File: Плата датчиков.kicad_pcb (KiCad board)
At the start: 2 copper layers, 66 x 58.4 mm, 23 parts, among them J1 A, J2 B, J3 C

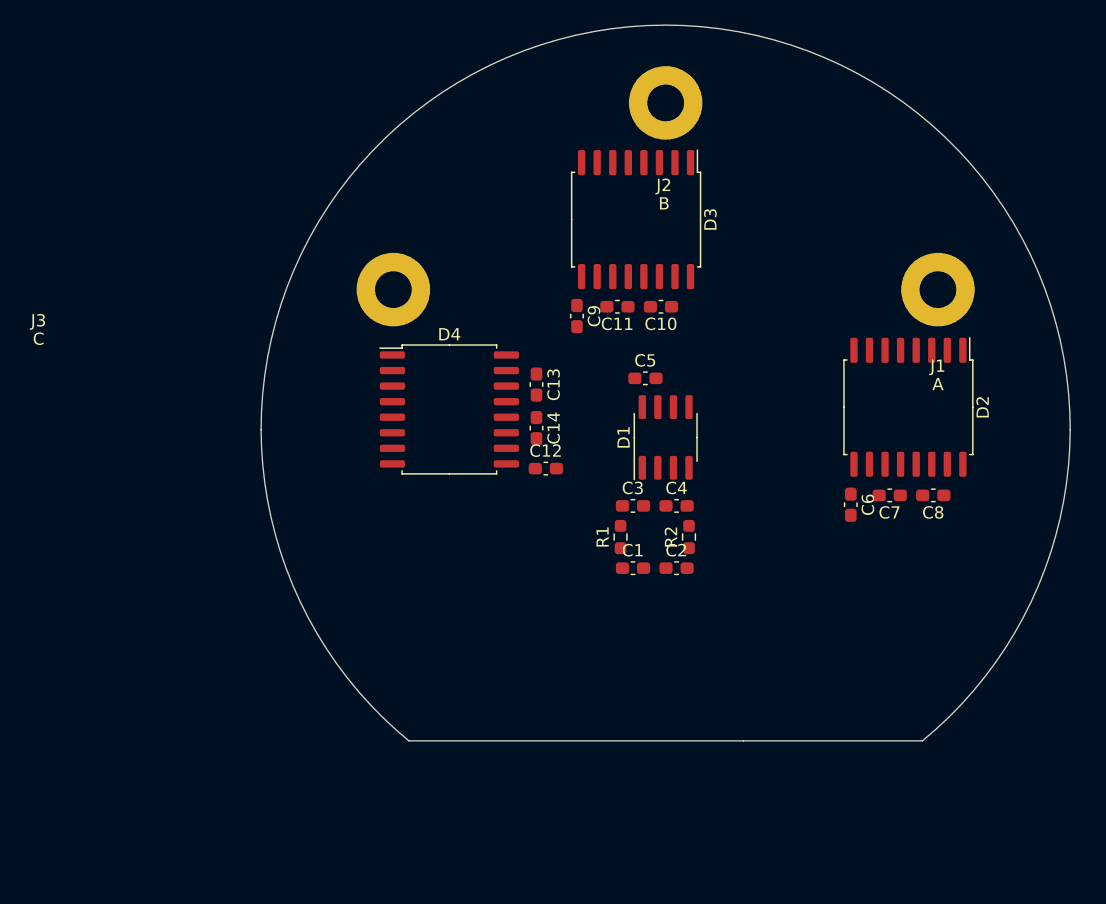
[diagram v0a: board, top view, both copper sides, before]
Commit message: Изменил контур под новую крышку
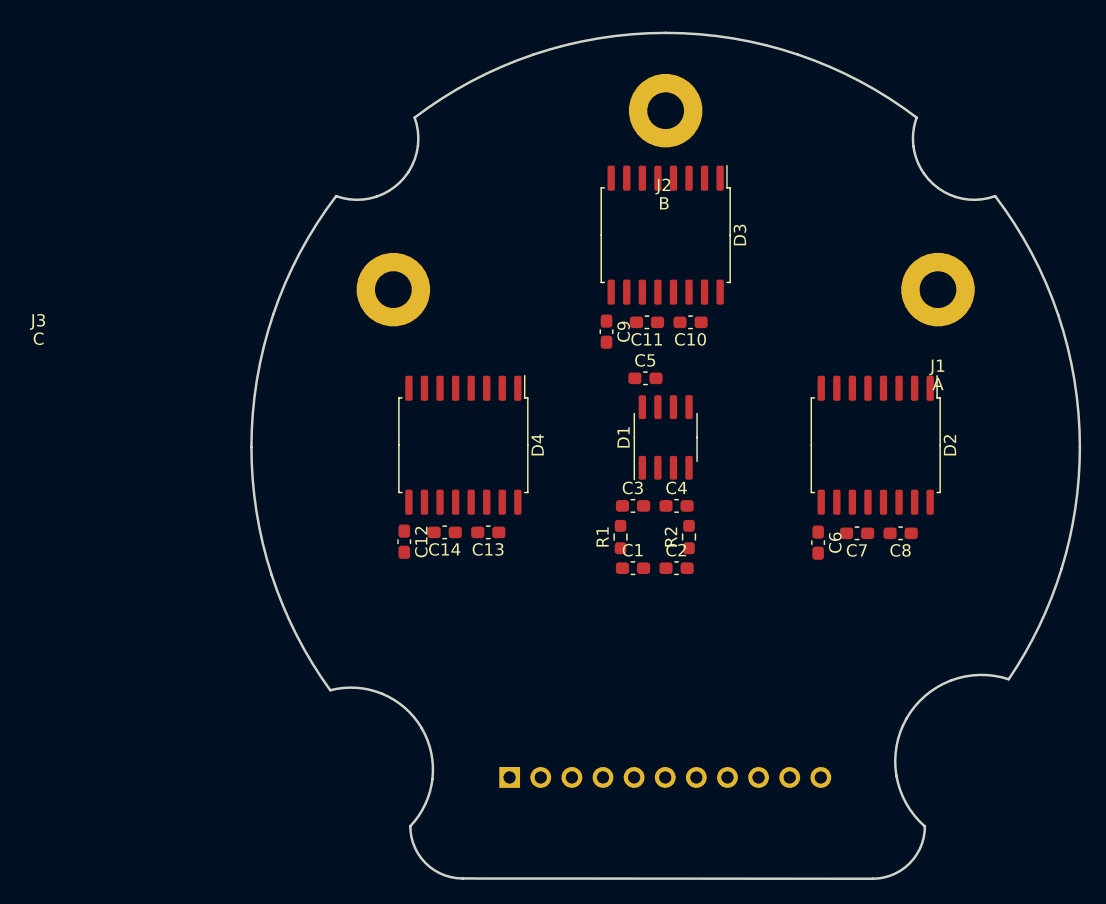
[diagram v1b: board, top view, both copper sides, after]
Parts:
- added J4: Conn_01x11, Connector_PinHeader_2.54mm:PinHeader_1x11_P2.54mm_Vertical, B.Cu at (70.5, 123.0)
- moved C12 13.0 mm to (61.8, 103.8), turned to -90 degrees
- moved C13 12.7 mm to (68.7, 103.0), turned to 180 degrees
- moved C14 11.3 mm to (65.2, 103.0), turned to 180 degrees
- moved C6 4.09 mm to (95.6, 103.8)
- moved C7 4.09 mm to (98.8, 103.1)
- moved C8 4.09 mm to (102.4, 103.1)
- moved D2 4.09 mm to (100.3, 95.9)
- moved D4 3.14 mm to (66.7, 95.9), turned to -90 degrees
- moved C10 2.73 mm to (85.2, 85.9)
- moved C11 2.73 mm to (81.7, 85.9)
- moved C9 2.73 mm to (78.4, 86.6)
- moved D3 2.73 mm to (83.2, 78.7)
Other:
- board size 66 x 58.4 mm -> 67.6 x 69 mm

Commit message: Поменял датчики на шунты
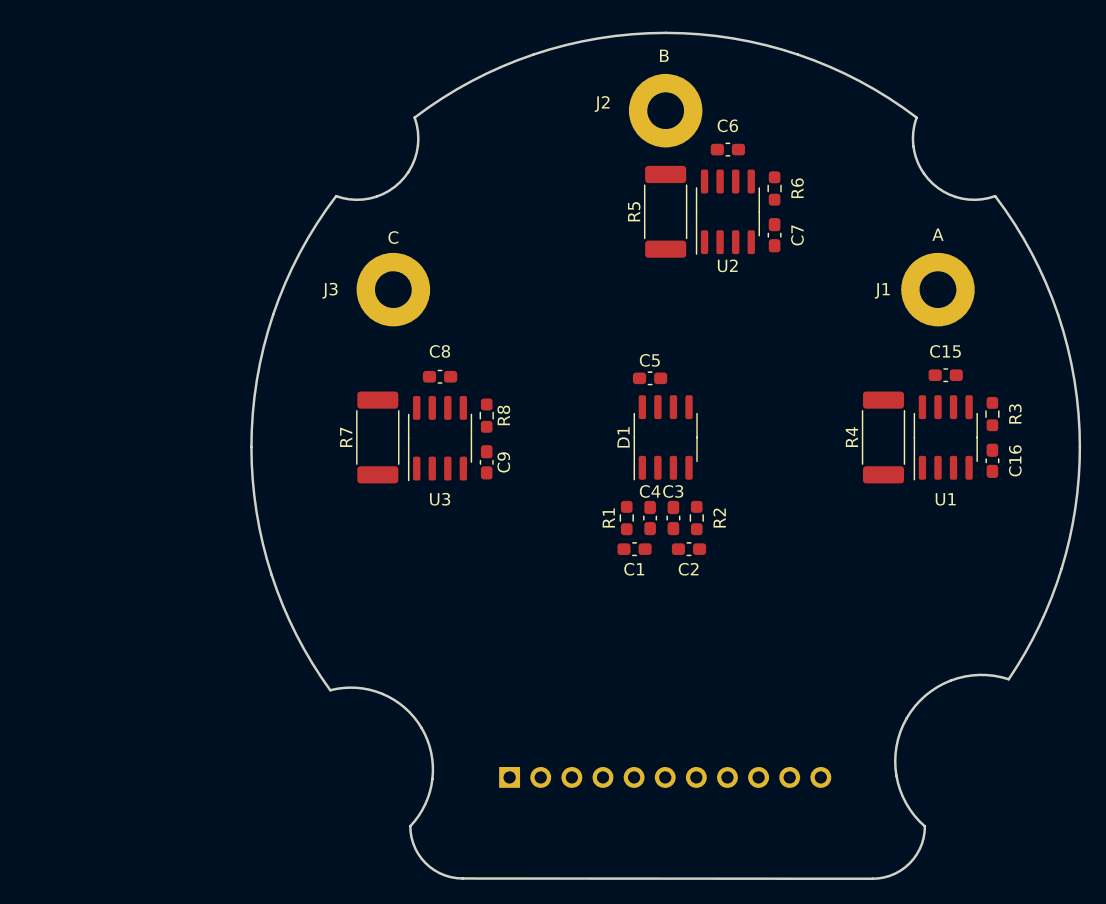
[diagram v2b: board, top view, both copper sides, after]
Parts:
- removed C10, C11, C13, C14: 1n, Capacitor_SMD:C_0603_1608Metric_Pad1.08x0.95mm_HandSolder
- removed C12: 10u, Capacitor_SMD:C_0603_1608Metric_Pad1.08x0.95mm_HandSolder
- removed D2, D3, D4: NSM2011, Package_SO:SOIC-16W_7.5x10.3mm_P1.27mm
- added C15: 0.1u, Capacitor_SMD:C_0603_1608Metric_Pad1.08x0.95mm_HandSolder, F.Cu at (106.0, 90.2)
- added C16: 56p, Capacitor_SMD:C_0603_1608Metric_Pad1.08x0.95mm_HandSolder, F.Cu at (109.9, 97.2)
- added R3: 120, Resistor_SMD:R_0603_1608Metric_Pad0.98x0.95mm_HandSolder, F.Cu at (109.9, 93.3)
- added R4: 0.5m, Resistor_SMD:R_2512_6332Metric_Pad1.40x3.35mm_HandSolder, F.Cu at (101.0, 95.2)
- added R5: 0.5m, Resistor_SMD:R_2512_6332Metric_Pad1.40x3.35mm_HandSolder, F.Cu at (83.2, 76.8)
- added R6: 120, Resistor_SMD:R_0603_1608Metric_Pad0.98x0.95mm_HandSolder, F.Cu at (92.1, 74.9)
- added R7: 0.5m, Resistor_SMD:R_2512_6332Metric_Pad1.40x3.35mm_HandSolder, F.Cu at (59.7, 95.2)
- added R8: 120, Resistor_SMD:R_0603_1608Metric_Pad0.98x0.95mm_HandSolder, F.Cu at (68.6, 93.5)
- added U1: INA283, Package_SO:SOIC-8_3.9x4.9mm_P1.27mm, F.Cu at (106.0, 95.2)
- added U2: INA283, Package_SO:SOIC-8_3.9x4.9mm_P1.27mm, F.Cu at (88.3, 76.8)
- added U3: INA283, Package_SO:SOIC-8_3.9x4.9mm_P1.27mm, F.Cu at (64.8, 95.3)
- C6: value 10u -> 0.1u
- C7: value 1n -> 56p
- C8: value 1n -> 0.1u
- C9: value 10u -> 56p
- moved C8 39.7 mm to (64.8, 90.3)
- moved C6 32.9 mm to (88.3, 71.8), turned to 180 degrees
- moved C7 25.2 mm to (92.1, 78.7), turned to -90 degrees
- moved C9 14.5 mm to (68.6, 97.3)
- moved C2 1.85 mm to (85.1, 104.4)
- moved C3 1.71 mm to (81.9, 101.8), turned to -90 degrees
- moved R2 1.68 mm to (85.7, 101.8)
- moved R1 1.63 mm to (80.0, 101.8)
- moved C1 1.56 mm to (80.6, 104.4)
- moved C4 1.02 mm to (83.8, 101.8), turned to 90 degrees
- moved C5 0.38 mm to (81.9, 90.4)
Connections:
- C7 pad 1: Current_A_MCU -> Current_B_MCU
- C8 pad 1: GND -> +3.3V
- C8 pad 2: Net-(D2-FILT) -> GND
- C9 pad 1: +3.3V -> Current_C_MCU

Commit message: Добавил разъёмы под обмотку
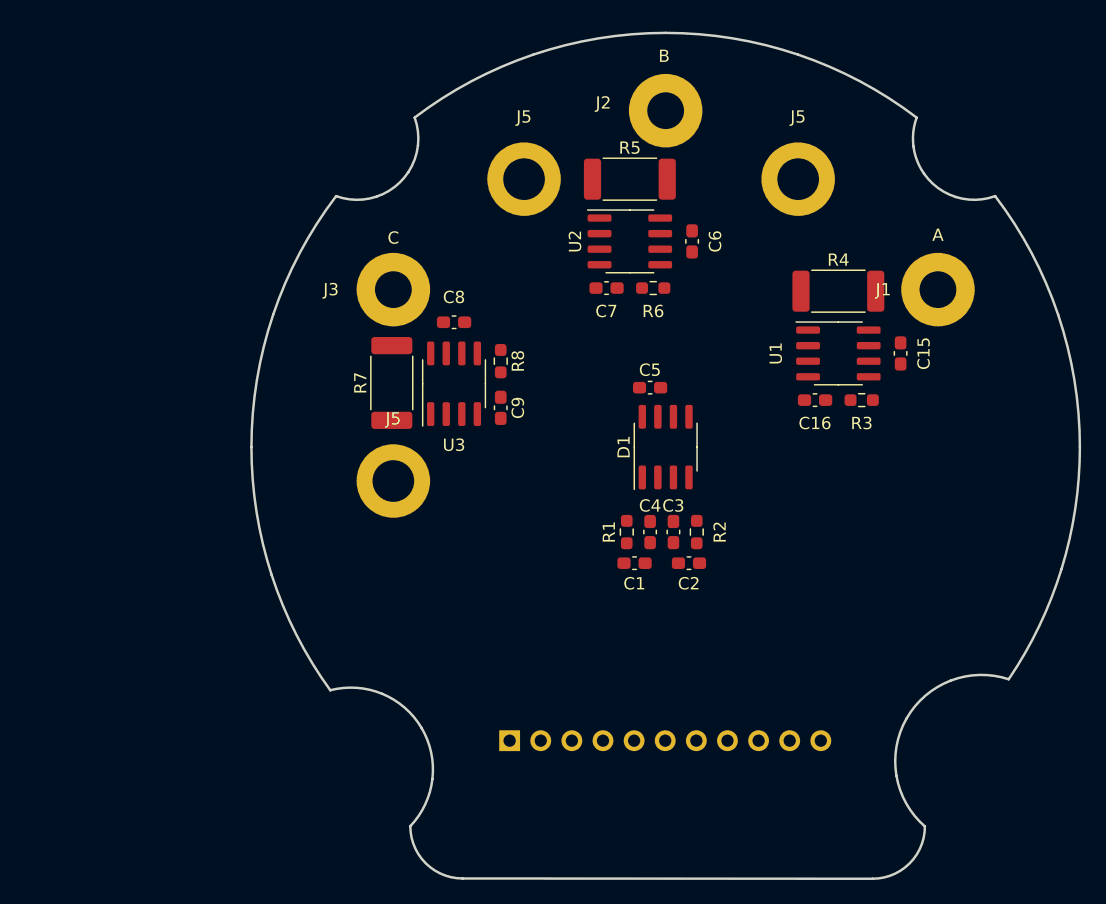
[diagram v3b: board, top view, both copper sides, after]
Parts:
- added J5: A, Connector_My:Power_Wire, F.Cu at (94.0, 74.2)
- added J5: A, Connector_My:Power_Wire, F.Cu at (71.6, 74.2)
- added J5: A, Connector_My:Power_Wire, F.Cu at (61.0, 98.8)
- moved C16 15.3 mm to (95.4, 92.2), turned to 180 degrees
- moved C7 14.4 mm to (78.4, 83.1), turned to 180 degrees
- moved R6 12.8 mm to (82.2, 83.1), turned to 0 degrees
- moved R4 12.5 mm to (97.3, 83.3), turned to 180 degrees
- moved U1 11.1 mm to (97.3, 88.4), turned to 0 degrees
- moved R3 10.7 mm to (99.2, 92.2), turned to 0 degrees
- moved U2 8.36 mm to (80.3, 79.2), turned to 0 degrees
- moved C6 8.04 mm to (85.3, 79.2), turned to 90 degrees
- moved C8 4.59 mm to (65.9, 85.8)
- moved C9 4.59 mm to (69.7, 92.8)
- moved R7 4.59 mm to (60.8, 90.8)
- moved R8 4.59 mm to (69.7, 89.0)
- moved U3 4.59 mm to (65.9, 90.9)
- moved C15 4.09 mm to (102.4, 88.4), turned to 90 degrees
- moved R5 3.96 mm to (80.3, 74.2), turned to 180 degrees
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
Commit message: Переместил силовые разъёмы
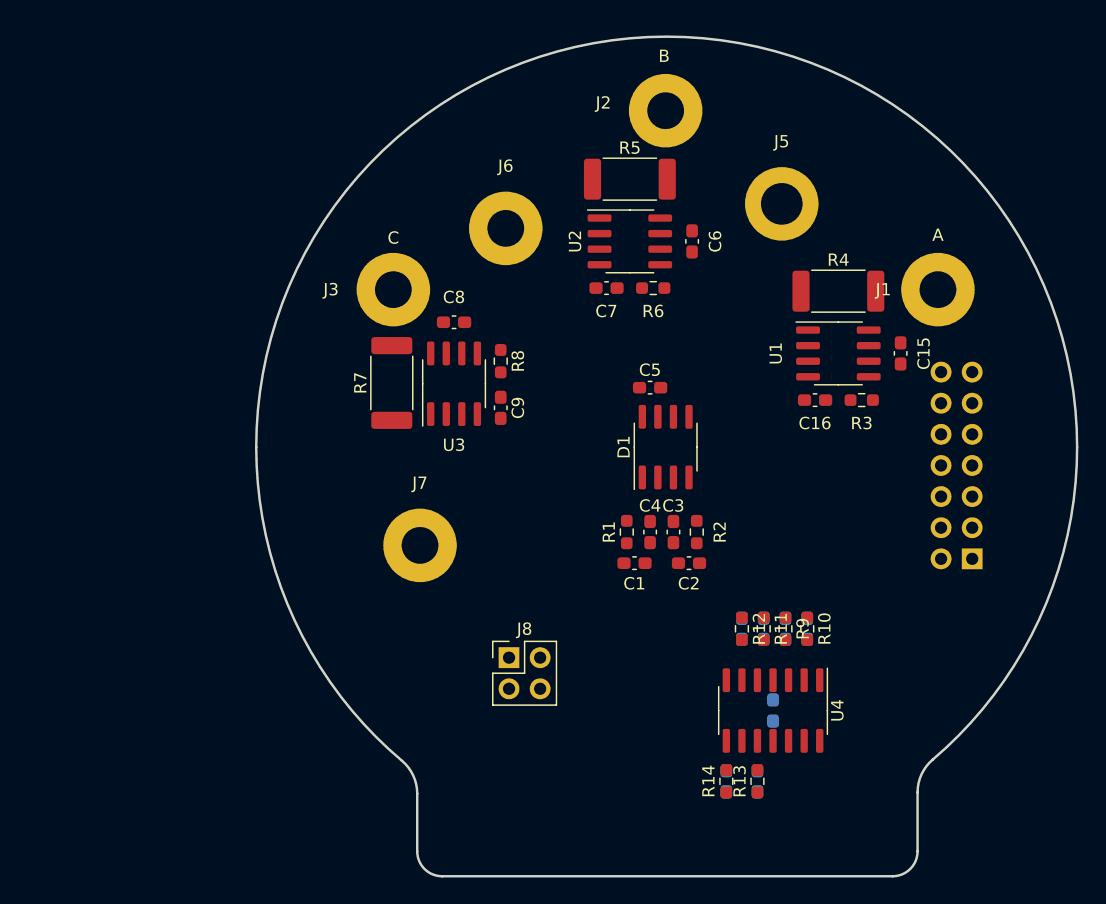
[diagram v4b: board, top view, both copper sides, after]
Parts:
- removed the J5 at (94.0, 74.2)
- removed the J5 at (61.0, 98.8)
- added C10: 100n, Capacitor_SMD:C_0603_1608Metric_Pad1.08x0.95mm_HandSolder, B.Cu at (93.0, 110.9)
- added C11: 100n, Capacitor_SMD:C_0603_1608Metric_Pad1.08x0.95mm_HandSolder, B.Cu at (94.7, 110.9)
- added C12: 100n, Capacitor_SMD:C_0603_1608Metric_Pad1.08x0.95mm_HandSolder, B.Cu at (91.2, 110.9)
- added C13: 100n, Capacitor_SMD:C_0603_1608Metric_Pad1.08x0.95mm_HandSolder, B.Cu at (89.4, 110.9)
- added C14: 100n, Capacitor_SMD:C_0603_1608Metric_Pad1.08x0.95mm_HandSolder, B.Cu at (90.7, 123.3)
- added C17: 100n, Capacitor_SMD:C_0603_1608Metric_Pad1.08x0.95mm_HandSolder, B.Cu at (88.1, 123.3)
- added C18: 0.1u, Capacitor_SMD:C_0603_1608Metric_Pad1.08x0.95mm_HandSolder, B.Cu at (91.9, 117.5)
- added J6: B_OUT, Connector_My:Power_Wire, F.Cu at (70.1, 78.2)
- added J7: C_OUT, Connector_My:Power_Wire, F.Cu at (63.1, 104.1)
- added J8: Conn_02x02_Odd_Even, Connector_PinHeader_2.54mm:PinHeader_2x02_P2.54mm_Vertical, F.Cu at (70.4, 113.2)
- added R10: 120, Resistor_SMD:R_0603_1608Metric_Pad0.98x0.95mm_HandSolder, F.Cu at (94.7, 110.9)
- added R11: 1.5k, Resistor_SMD:R_0603_1608Metric_Pad0.98x0.95mm_HandSolder, F.Cu at (91.2, 110.9)
- added R12: 120, Resistor_SMD:R_0603_1608Metric_Pad0.98x0.95mm_HandSolder, F.Cu at (89.4, 110.9)
- added R13: 1.5k, Resistor_SMD:R_0603_1608Metric_Pad0.98x0.95mm_HandSolder, F.Cu at (90.7, 123.3)
- added R14: 120, Resistor_SMD:R_0603_1608Metric_Pad0.98x0.95mm_HandSolder, F.Cu at (88.1, 123.3)
- added R9: 1.5k, Resistor_SMD:R_0603_1608Metric_Pad0.98x0.95mm_HandSolder, F.Cu at (93.0, 110.9)
- added U4: LMV324, Package_SO:SOIC-14_3.9x8.7mm_P1.27mm, F.Cu at (91.9, 117.5)
- J4: value Conn_01x11 -> Conn_02x07_Odd_Even; footprint Connector_PinHeader_2.54mm:PinHeader_1x11_P2.54mm_Vertical -> Connector_PinSocket_2.54mm:PinSocket_2x07_P2.54mm_Vertical
- J5: value A -> A_OUT
- moved J4 40.6 mm to (108.2, 105.2), turned to 0 degrees
- moved J5 21.1 mm to (92.7, 76.2)
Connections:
- J4 pad 1: GND -> +3.3V
- J4 pad 10: GND -> Temp_Coil_A_MCU
- J4 pad 11: Current_A_MCU -> Current_B_MCU
- J4 pad 2: Current_C_MCU -> GND
- J4 pad 3: GND -> SCLK_MCU
- J4 pad 4: +3.3V -> GNDA
- J4 pad 5: SCLK_MCU -> CS_MCU
- J4 pad 6: CS_MCU -> Temp_Coil_C_MCU
- J4 pad 8: GND -> Temp_Coil_B_MCU
- J4 pad 9: Current_B_MCU -> Current_C_MCU
- J5 pad 1: (no net) -> A_OUT
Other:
- board size 67.6 x 69 mm -> 67 x 68.5 mm

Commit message: С ножевыми разъёмами по кругу
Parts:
- added J10: 4900, Connector_My:4900, F.Cu at (74.2, 78.4)
- added J11: 4900, Connector_My:4900, F.Cu at (70.9, 81.8)
- added J12: 4900, Connector_My:4900, F.Cu at (60.5, 99.1)
- added J13: 4900, Connector_My:4900, F.Cu at (61.9, 104.7)
- added J14: 4900, Connector_My:4900, F.Cu at (65.0, 109.8)
- added J9: 4900, Connector_My:4900, F.Cu at (88.8, 77.9)
- C15, C6, C8: moved to B.Cu
- J5: value A_OUT -> 4900; footprint Connector_My:Power_Wire -> Connector_My:4900
- J6: value B_OUT -> 4900; footprint Connector_My:Power_Wire -> Connector_My:4900
- J7: value C_OUT -> 4900; footprint Connector_My:Power_Wire -> Connector_My:4900
- moved J7 30.7 mm to (78.8, 77.6), turned to 105 degrees
- moved J6 26.8 mm to (96.5, 83.1), turned to 45 degrees
- moved R3 11.5 mm to (89.2, 97.9), turned to -90 degrees
- moved C15 10.7 mm to (93.0, 93.5), turned to 0 degrees
- moved U1 8.76 mm to (93.0, 96.0), turned to -90 degrees
- moved C8 7.29 mm to (72.6, 88.6)
- moved C9 6.86 mm to (76.6, 93.1)
- moved R8 6.86 mm to (76.6, 89.3)
- moved R7 6.74 mm to (67.6, 91.2)
- moved U3 6.74 mm to (72.6, 91.1)
- moved C16 6.51 mm to (89.2, 94.1), turned to 90 degrees
- moved C7 5.92 mm to (81.4, 88.1)
- moved R6 5.92 mm to (85.2, 88.1)
- moved U2 5.80 mm to (83.1, 84.3)
- moved C6 5.09 mm to (85.6, 84.3)
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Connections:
- J6 pad 1: B_OUT -> A_OUT
- J7 pad 1: C_OUT -> B_OUT

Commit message: Расставил ножевые разъмы финально
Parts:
- C15, C6: moved to F.Cu
- C16, C7, R3, R4, R5, R6, U1, U2: moved to B.Cu
- moved J9 36.8 mm to (89.6, 114.7), turned to -70 degrees
- moved J5 32.6 mm to (94.2, 112.3), turned to -55 degrees
- moved J6 25.6 mm to (98.0, 108.7), turned to -40 degrees
- moved J10 18.3 mm to (92.5, 79.0), turned to 60 degrees
- moved J7 18.2 mm to (96.5, 82.1), turned to 45 degrees
- moved J11 17.4 mm to (87.6, 77.1), turned to 75 degrees
- moved Je 15.3 mm to (59.6, 89.6), turned to -15 degrees
- moved R4 11.2 mm to (100.9, 99.1), turned to -90 degrees
- moved C10 10.4 mm to (82.5, 111.5)
- moved C11 10.4 mm to (84.3, 111.5)
- moved C12 10.4 mm to (80.8, 111.5)
- moved C13 10.4 mm to (79.0, 111.5)
- moved C14 10.4 mm to (80.3, 124.0)
- moved C17 10.4 mm to (77.7, 124.0)
- moved R10 10.4 mm to (84.3, 111.5)
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- renumbered J13 to Je
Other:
- copper layers 2 -> 4
